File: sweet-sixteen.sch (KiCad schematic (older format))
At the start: 71 parts

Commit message: update docs
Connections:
- net at U?.23 (R-EXT): now also R?.2
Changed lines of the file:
@@
 	2300 7500 2300 7600
 Wire Wire Line
-	14250 1900 14250 1900
+	14250 1900 14400 1900
 Wire Wire Line
 	10200 7500 10350 7500
@@
 	14250 8000 14250 7500
 Wire Wire Line
-	1000 8250 1200 8250
-Wire Wire Line
-	1200 8250 3050 8250
-Wire Wire Line
-	3050 8250 4900 8250
-Wire Wire Line
-	4900 8250 6750 8250
-Wire Wire Line
-	6750 8250 8900 8250
-Wire Wire Line
-	8900 8250 10750 8250
-Wire Wire Line
-	10750 8250 12600 8250
-Wire Wire Line
-	12600 8250 14450 8250
-Wire Wire Line
-	14450 8250 15950 8250
-Wire Wire Line
-	1000 8100 1100 8100
-Wire Wire Line
-	1100 8100 2950 8100
-Wire Wire Line
-	2950 8100 4800 8100
-Wire Wire Line
-	4800 8100 6650 8100
-Wire Wire Line
-	6650 8100 8800 8100
-Wire Wire Line
-	8800 8100 10650 8100
-Wire Wire Line
-	10650 8100 12500 8100
-Wire Wire Line
-	12500 8100 14350 8100
-Wire Wire Line
-	14350 8100 15850 8100
+	1000 8250 15950 8250
+Wire Wire Line
+	1000 8100 15850 8100
 Wire Wire Line
 	15750 7950 14550 7950
@@
 	11900 2450 11900 2600
 Wire Wire Line
-	10000 2450 10350 2450
-Wire Wire Line
-	10350 2450 10550 2450
-Wire Wire Line
-	10550 2450 10750 2450
-Wire Wire Line
-	10750 2450 10950 2450
-Wire Wire Line
-	10950 2450 11300 2450
-Wire Wire Line
-	11300 2450 11500 2450
-Wire Wire Line
-	11500 2450 11700 2450
-Wire Wire Line
-	11700 2450 11900 2450
+	10000 2450 11900 2450
 Connection ~ 10350 2450
 Connection ~ 10550 2450
@@
 	15750 1400 15750 7950
 Wire Wire Line
-	15850 8100 15850 1300
-Wire Wire Line
-	15950 8250 15950 1200
-Wire Wire Line
-	14050 1400 14550 1400
-Wire Wire Line
-	14550 1400 15750 1400
+	15850 1300 15850 8100
+Wire Wire Line
+	15950 1200 15950 8250
+Wire Wire Line
+	14050 1400 15750 1400
 Wire Wire Line
 	14050 1400 14050 1900
 Wire Wire Line
-	15950 1200 15150 1200
-Wire Wire Line
-	15150 1200 13850 1200
+	13850 1200 15950 1200
 Wire Wire Line
 	13750 600  15450 600
@@
 	5600 1150 5750 1150
 Wire Wire Line
-	5600 9350 5600 9450
-Wire Wire Line
-	5600 9450 5600 9550
+	5600 9350 5600 9550
 Connection ~ 5600 9450
 Wire Wire Line
@@
 	3800 9900 5600 9900
 Wire Wire Line
-	5600 9800 5600 9900
-Wire Wire Line
-	5600 9900 5600 10000
+	5600 9800 5600 10000
 Connection ~ 5600 9900
 Wire Wire Line
-	5600 10250 5600 10350
-Wire Wire Line
-	5600 10350 5600 10450
+	5600 10250 5600 10450
 Wire Wire Line
 	5600 10350 5450 10350
@@
 	11100 1750 11200 1750
 Wire Wire Line
-	1300 9600 1350 9600
-Wire Wire Line
-	1350 9600 1400 9600
-Wire Wire Line
-	1600 9600 1650 9600
-Wire Wire Line
-	1650 9600 1700 9600
+	1300 9600 1400 9600
+Wire Wire Line
+	1600 9600 1700 9600
 Wire Wire Line
 	1400 9900 1350 9900
@@
 	13950 1900 13950 1300
 Wire Wire Line
-	13950 1300 15050 1300
-Wire Wire Line
-	15050 1300 15850 1300
+	13950 1300 15850 1300
 Wire Wire Line
 	15150 900  15150 1200
@@
 	13850 1200 13850 1900
 Wire Wire Line
-	13750 600  13750 950
-Wire Wire Line
-	13750 950  13750 1900
+	13750 600  13750 1900
 Connection ~ 13750 950
 Wire Wire Line
@@
 	13750 950  13850 950
 Wire Wire Line
-	14250 1900 14400 1900
-Wire Wire Line
-	14400 1900 14400 1900
+	3800 7500 3750 7500
 $EndSCHEMATC

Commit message: redo schematic layout, pi interface, add output line driver, connect oe
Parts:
- removed C?: 10nf, symbol C_Small
- removed JP1: JUMPER, symbol JUMPER
- removed P?: RPI_IF, symbol CONN_02X40
- removed R?: R, symbol R
- added C?: 10nf, symbol C_Small
- added P?: ~OE_I, symbol CONN_01X01
- added P?: ~OE_O, symbol CONN_01X01
- added P?: CONN_02X20, symbol CONN_02X20
- added R?: 1k, symbol R
- added U? (x4): 74LS08, symbol 74LS08
- R? (x8): value R -> 1k
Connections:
- net CLK: now also U?.6, U?.4, U?.5; no longer P?.1 (P1), U?.3
- net GND: now also U?.1 (GND), C?.2, P?.14 (P14), P?.20 (P20), P?.25 (P25), P?.30 (P30), P?.34 (P34), P?.35 (P35), P?.39 (P39), P?.6 (P6), P?.9 (P9), R?.1, U?.7 (GND), U?.7 (GND), U?.7 (GND), U?.7 (GND)
- net LE: now also U?.11, U?.10, U?.9; no longer P?.1 (P1), U?.8
- net SDA: now also U?.8; no longer U?.6
- net VCC: now also C?.1, U?.14 (VCC), U?.14 (VCC), U?.14 (VCC), U?.14 (VCC); no longer U?.24 (VDD)
- net ~OE: now reaches U?.21 (~OE)
- net ~OE: now also U?.21 (~OE), U?.21 (~OE), U?.21 (~OE), U?.21 (~OE), U?.21 (~OE), U?.21 (~OE), U?.21 (~OE), U?.21 (~OE), U?.3, P?.1 (P1), U?.12, U?.13
- net at U?.22 (SDO): now also U?.1, U?.2; no longer P?.1 (P1)
- net at U?.23 (R-EXT): now also R?.2
- net PI_SDA: now reaches U?.10, U?.9
- net PI_SDA: now also P?.19 (P19)
- net PI_CLK: now reaches U?.4, U?.5
- net PI_CLK: now also P?.23 (P23)
- net V_PI: now reaches F?.1
- net V_PI: now also P?.2 (P2), P?.4 (P4)
- net ~PI_OE: now reaches U?.1, U?.2
- net ~PI_OE: now also P?.12 (P12)
- net PI_LE: now reaches U?.12, U?.13
- net PI_LE: now also P?.15 (P15)
- new net: P?.1 (P1), U?.3
- new net: P?.1 (P1), U?.6
- new net: P?.1 (P1), U?.8
- new net: P?.1 (P1), U?.11
- no-connect marks 1 -> 0
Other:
- note removed: "Note: 8th Driver for Decimal Points\nand Aux-LEDs might not be populated.\nThen, JP1 must be bridged to connedt\nSDA to SDO directly"
- moved on the sheet: AFF?, C?, D?, F?, P?, R?, U?, U?A, U?B, U?C, U?D

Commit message: redo power section, make erc pass
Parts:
- removed U? (x2): LM7808ACT, TO-220, symbol LM7808ACT
- added F1, F3: 1.2A F, symbol F_Small
- added JP1, JP3: JUMPER3, symbol JUMPER3
- added JP2, JP4, JP5: JUMPER, symbol JUMPER
- added R10, R12: 1.2k, symbol R
- added R11, R13: 680, symbol R
- added U1, U3: OKI-T/3-W40, symbol OKI-T/3
- F2: renamed from F?; value 500mA -> 2.5A S
- P10: renamed from P?; value 12V_O -> VIN_O
- P7: renamed from P?; value 12V_I -> VIN_I
- U13, U5: renamed from U?; value 74LS08 -> 74HCT08
- W1: renamed from W?; value VLED -> VLED=4.4V
- W2: renamed from W?; value +12V -> VIN=16V-40V
- W3: renamed from W?; value +5V -> VCC=5V
- gave numbers to parts that had none: 59
- renumbered CON_PWR to CON_PWR1
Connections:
- net GND: now also CON_PWR1.3, JP1.1, JP3.1, R11.2, R13.2, U1.3 (GND), U3.3 (GND)
- net VCC: now also U12.24 (VDD), JP4.2
- net VLED: now also JP2.2
- net VIN: now reaches P10.1 (P1)
- net VIN: now also P7.1 (P1), W2.1, F1.1, F3.1, JP1.3, JP3.3, JP5.2
- removed net +12V: CON_PWR1.1, P7.1 (P1), W2.1
- new net: CON_PWR1.1, JP5.1
- new net: JP1.2, U1.1 (OnOff)
- new net: F1.2, U1.2 (VIN)
- new net: R10.2, U1.4 (Trim)
- new net: JP2.1, U1.5 (VOUT)
- new net: JP3.2, U3.1 (OnOff)
- new net: F3.2, U3.2 (VIN)
- new net: R12.2, U3.4 (Trim)
- new net: JP4.1, U3.5 (VOUT)
- new net: R10.1, R11.1
- new net: R12.1, R13.1
- no-connect marks 0 -> 25
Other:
- note added: "Note:\n6A Capable Trace between\nVIN_I/O, GND_I/O and CON_PWR"
- note added: "Note:\nOn the first Board, CON_PWR and the 5V Power Module is populated.\nThe 5V (VCC) generated here from is then\npassed on to the other boards, together with V_IN.\nV_LED is generated on each Board separately from V_IN.\nThe Jumer on ONOFF are for positive/negative module selection.\nThe Jumer on the outputs are for In-Situ Current Measurement."
- note added: "Note:\nThe HCT-Type Gate here is used as a Level-Shifter\nfrom 3.3V to 5V, so it is important to use a HCT-Type\nGate (not HC/AC/LS or other Type)"
- note added: "VCC"
- note added: "VIN"
- note added: "VLED"
- note removed: "Note: 7805 are only examples here,\nneed to be replaced with proper\nDC-DC converters, once the required\nvoltages and aperages are known"
- note removed: "Note: 8A Campable Trace between\n12V_I, 12VO resp. GND_I, GND_O\nand CON_PWR"
- moved on the sheet: C1, C2, CON_PWR1, F2, P10, P11, P5, P6, P7, P8, P9, U5A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

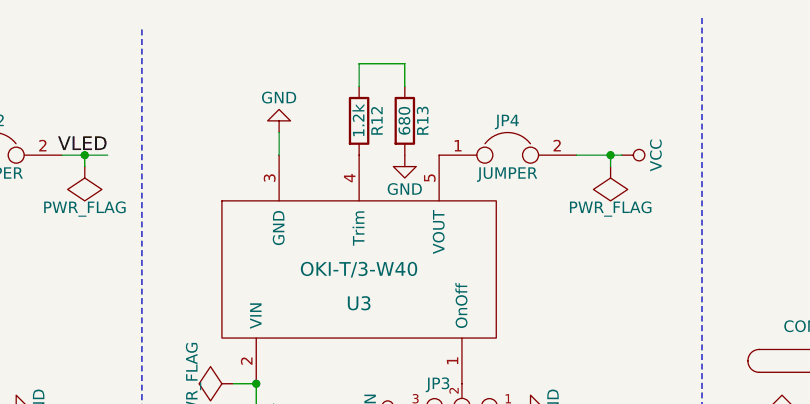
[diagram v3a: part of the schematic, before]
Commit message: update r value for trimming the vcc converter
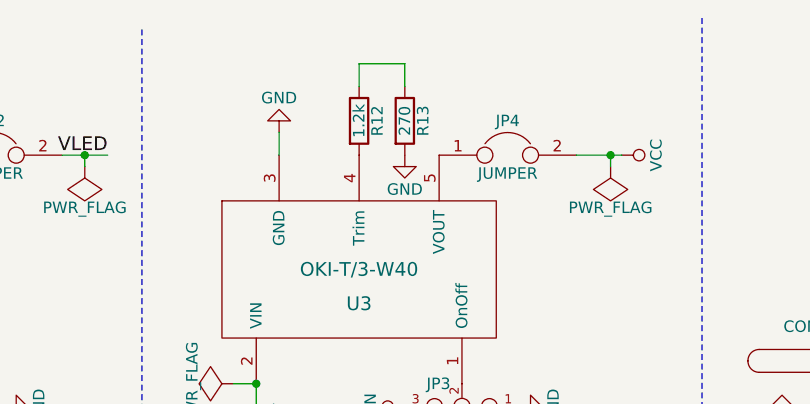
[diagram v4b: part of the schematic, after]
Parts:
- R13: value 680 -> 270
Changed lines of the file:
@@
-$EndComp
-$Comp
-L JUMPER3 JP1
-U 1 1 58AFEE9F
-P 1850 2100
-F 0 "JP1" H 1900 2000 50  0000 L CNN
-F 1 "JUMPER3" H 1850 2200 50  0000 C BNN
-F 2 "" H 1850 2100 50  0000 C CNN
-F 3 "" H 1850 2100 50  0000 C CNN
-	1    1850 2100
-	-1   0    0    1
 $EndComp
 $Comp
@@
 F 3 "" H 4350 2100 50  0000 C CNN
 	1    4350 2100
-	0    -1   -1   0
-$EndComp
-$Comp
-L GND #PWR062
-U 1 1 58AFF3FA
-P 2100 2100
-F 0 "#PWR062" H 2100 1850 50  0001 C CNN
-F 1 "GND" H 2100 1950 50  0000 C CNN
-F 2 "" H 2100 2100 50  0000 C CNN
-F 3 "" H 2100 2100 50  0000 C CNN
-	1    2100 2100
 	0    -1   -1   0
 $EndComp
@@
 P 3850 850
 F 0 "R13" V 3930 850 50  0000 C CNN
-F 1 "680" V 3850 850 50  0000 C CNN
+F 1 "270" V 3850 850 50  0000 C CNN
 F 2 "" V 3780 850 50  0000 C CNN
 F 3 "" H 3850 850 50  0000 C CNN
@@
 Text Notes 6600 2600 2    60   ~ 0
 VIN
+$Comp
+L GND #PWR062
+U 1 1 58AFF3FA
+P 2100 2100
+F 0 "#PWR062" H 2100 1850 50  0001 C CNN
+F 1 "GND" H 2100 1950 50  0000 C CNN
+F 2 "" H 2100 2100 50  0000 C CNN
+F 3 "" H 2100 2100 50  0000 C CNN
+	1    2100 2100
+	0    -1   -1   0
+$EndComp
+$Comp
+L JUMPER3 JP1
+U 1 1 58AFEE9F
+P 1850 2100
+F 0 "JP1" H 1900 2000 50  0000 L CNN
+F 1 "JUMPER3" H 1850 2200 50  0000 C BNN
+F 2 "" H 1850 2100 50  0000 C CNN
+F 3 "" H 1850 2100 50  0000 C CNN
+	1    1850 2100
+	-1   0    0    1
+$EndComp
 $EndSCHEMATC

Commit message: setup footprints for jumper and assign known footprints
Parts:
- C1, C10, C11, C2, C3, C4, C5, C6, C7, C8, C9: footprint (none) -> Capacitors_SMD:C_0805_HandSoldering
- D1, D2, D3, D4, D5, D6, D7, D8: footprint (none) -> LEDs:LED-5MM
- F1, F2, F3: footprint (none) -> SMD_Packages:SMD-2112_Pol
- JP1, JP3: footprint (none) -> jumper:SMD_Jumper_3
- JP2, JP4, JP5: footprint (none) -> jumper:SMD_Jumper_2
- P1, P10, P11, P12, P13, P14, P15, P2, P3, P4, P6, P7, P8, P9: footprint (none) -> SMD_Packages:1Pin
- P5: footprint (none) -> Pin_Headers:Pin_Header_Straight_2x20
- R1, R10, R11, R12, R13, R2, R3, R4, R5, R6, R7, R8, R9: footprint (none) -> Resistors_SMD:R_1206_HandSoldering
- U10, U11, U12, U2, U4, U6, U7, U8, U9: footprint (none) -> SMD_Packages:SOIC-24
- U13, U5: footprint (none) -> SMD_Packages:SOIC-14_N
- W1, W2, W3, W4: footprint (none) -> Measurement_Points:Measurement_Point_Round-SMD-Pad_Big

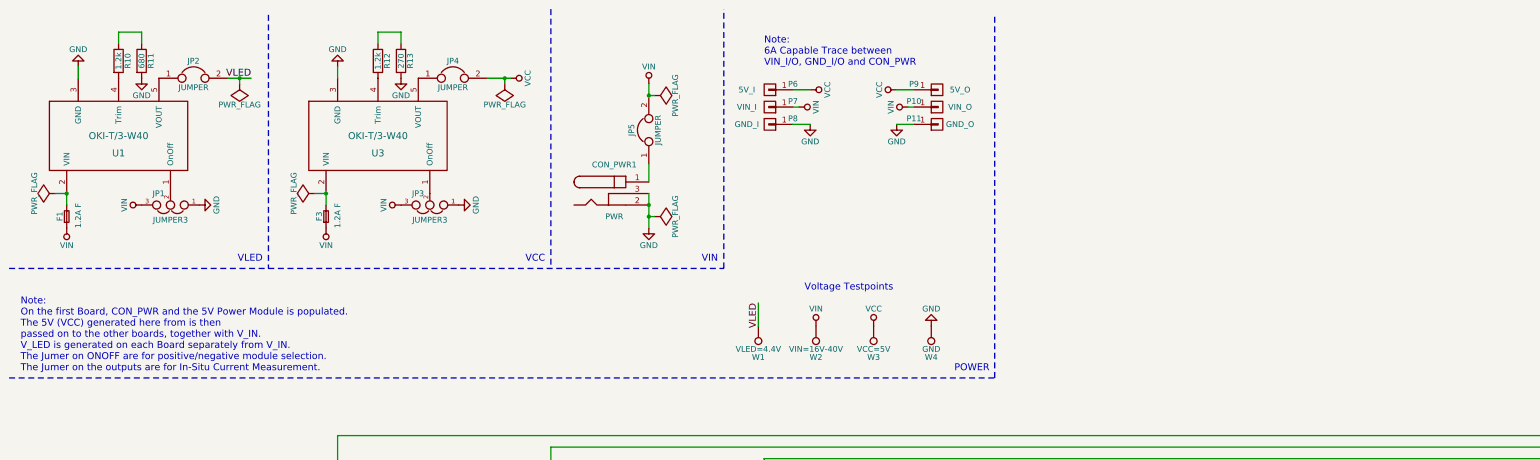
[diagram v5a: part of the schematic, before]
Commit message: add note about Rtrim placement
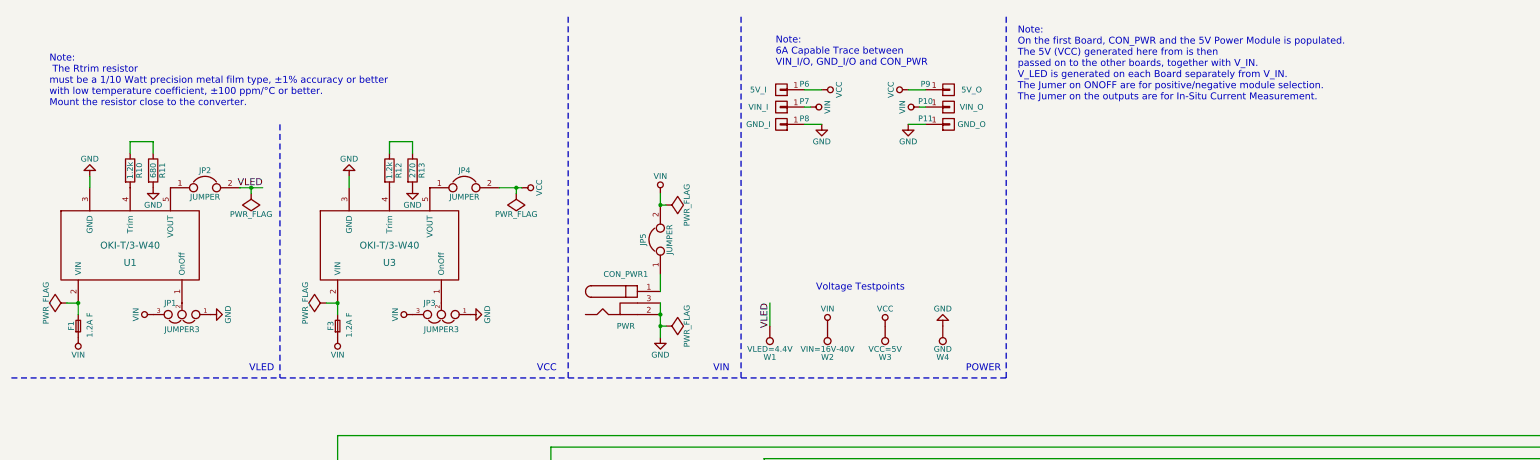
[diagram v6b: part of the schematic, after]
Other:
- note added: "Note:\n The Rtrim resistor\nmust be a 1/10 Watt precision metal film type, ±1% accuracy or better\nwith low temperature coefficient, ±100 ppm/°C or better.\nMount the resistor close to the converter."
- moved on the sheet: CON_PWR1, F1, F3, JP1, JP2, JP3, JP4, JP5, P10, P11, P6, P7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
